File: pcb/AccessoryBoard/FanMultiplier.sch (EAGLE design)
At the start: 22 parts

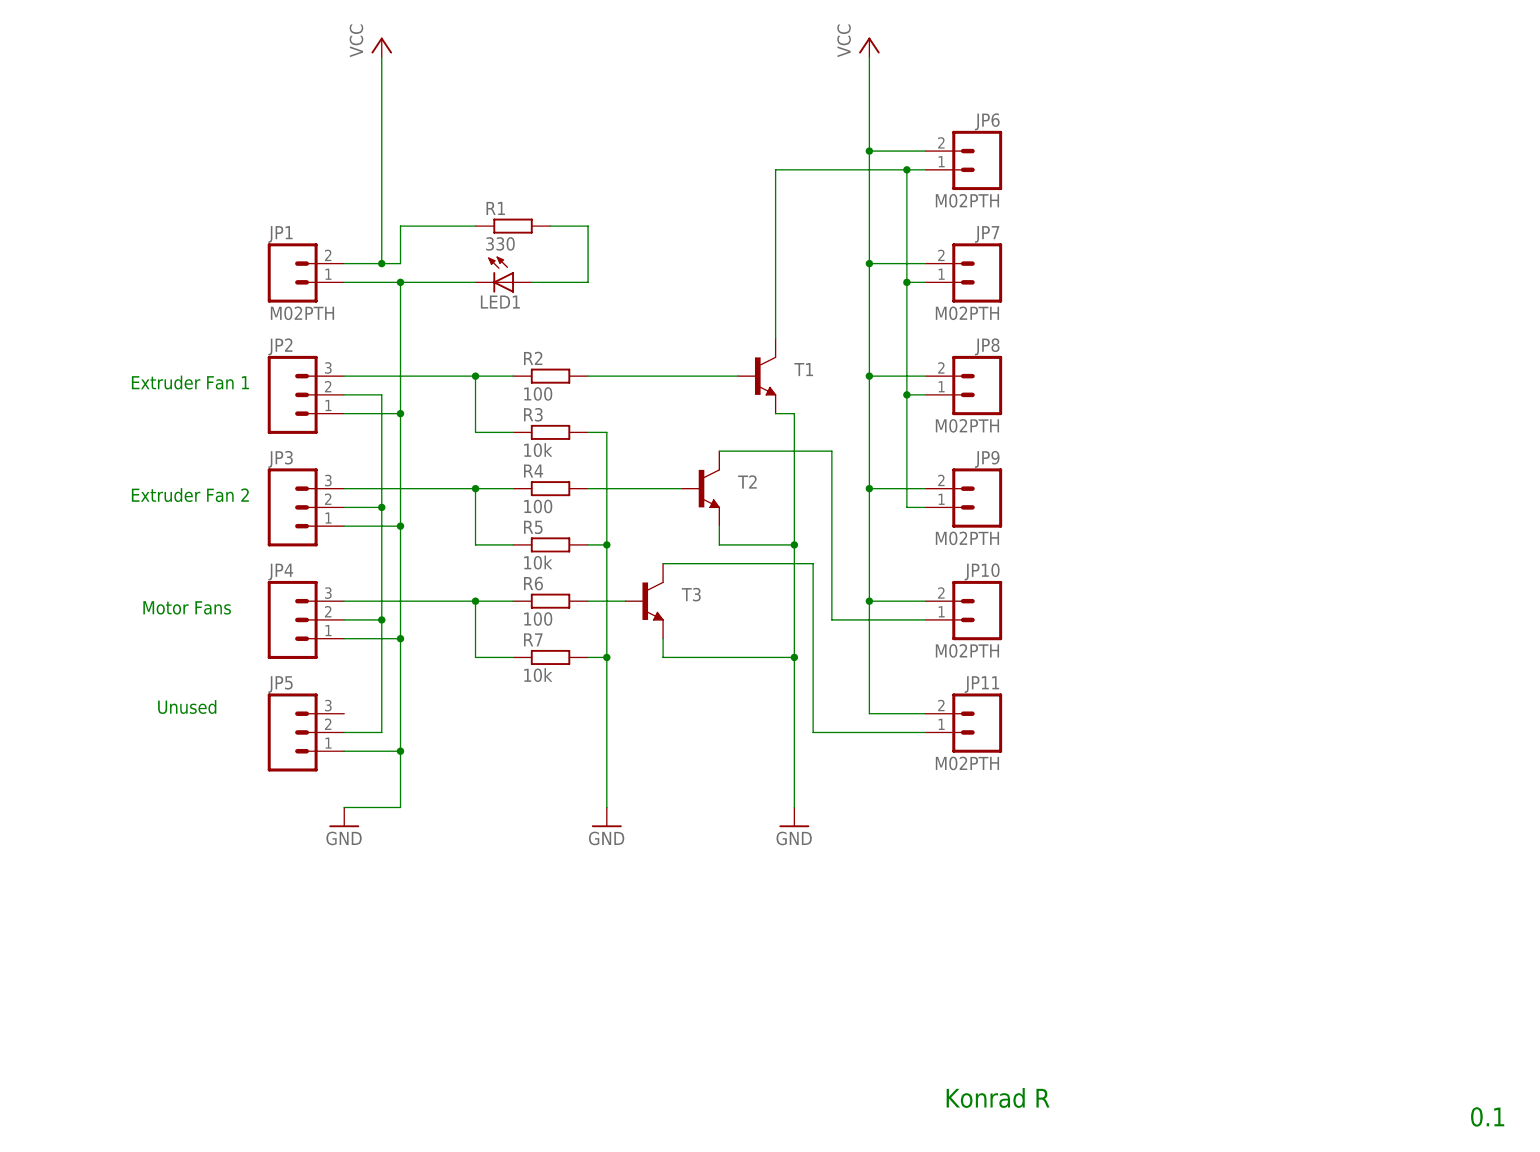
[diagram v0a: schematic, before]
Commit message: added vcc outputs added 4th pwm output
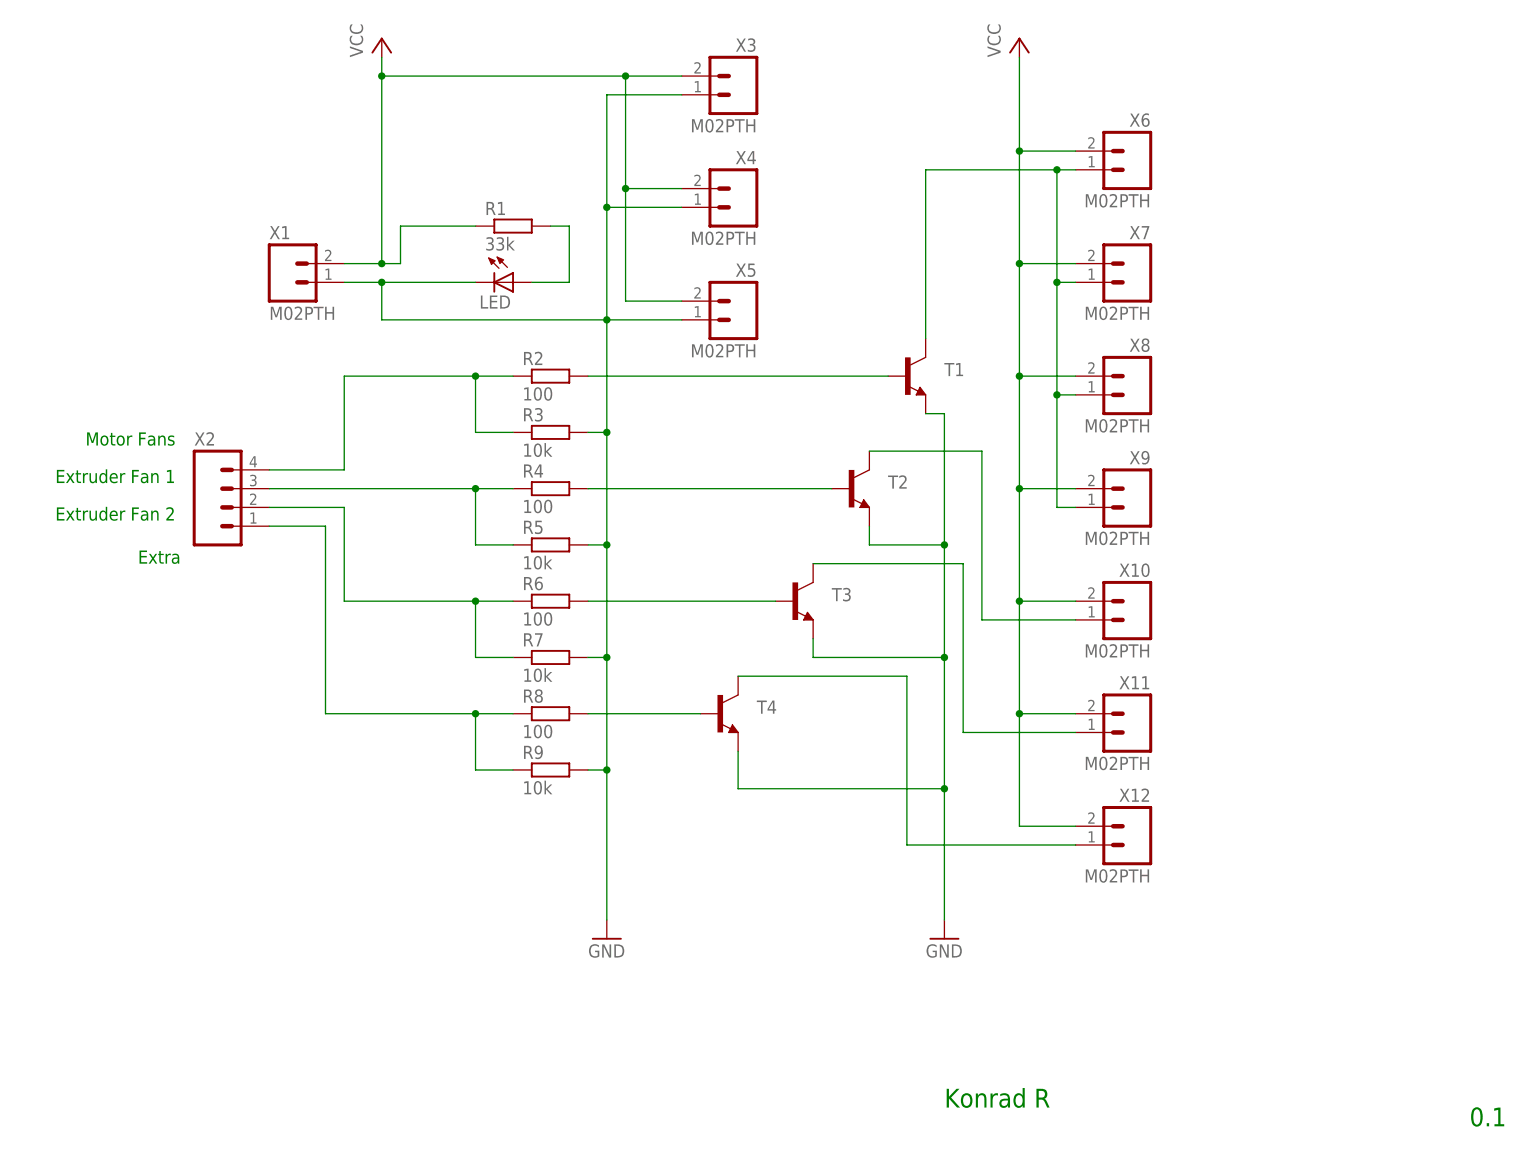
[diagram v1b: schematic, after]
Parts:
- removed JP10, JP11, JP6, JP7, JP8, JP9: M02PTH, SparkFun-Connectors:M02PTH
- removed JP2, JP3, JP4, JP5: (no value), SparkFun-Connectors:M03PTH
- added R8: 100, rcl:R-EU_0207/7
- added R9: 10k, rcl:R-EU_0207/7
- added T4: (no value), SparkFun-DiscreteSemi:TRANSISTOR_NPNTO92
- added X10, X11, X12, X3, X4, X5, X6, X7, X8, X9: M02PTH, SparkFun-Connectors:M02PTH
- added X2: (no value), SparkFun-Connectors:M04PTH
- R1: value 330 -> 33k
- renumbered JP1 to X1, LED1 to LED
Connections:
- new net N$11: R8.2, T4.B
- new net N$12: T4.C, X12.1
- net GND: now also R9.2, T4.E, X3.1, X4.1, X5.1; no longer JP2.1, JP3.1, JP4.1, JP5.1
- net N$14: now also X6.1, X7.1, X8.1, X9.1; no longer JP6.1, JP7.1, JP8.1, JP9.1
- net N$16: now also X10.1; no longer JP10.1
- net N$17: now also X11.1; no longer JP11.1
- net N$5: now also X2.4; no longer JP2.3
- net N$6: now also X2.3; no longer JP3.3
- net N$7: now also X2.2; no longer JP4.3
- net N$8: now also R8.1, R9.1, X2.1; no longer JP2.2, JP3.2, JP4.2, JP5.2
- net VCC: now also X10.2, X11.2, X12.2, X3.2, X4.2, X5.2, X6.2, X7.2, X8.2, X9.2; no longer JP10.2, JP11.2, JP6.2, JP7.2, JP8.2, JP9.2
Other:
- note added: "Extra"
- note removed: "Unused"
- moved on the sheet: T1, T2, T3

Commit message: minor routing improvements
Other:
- note added: "Nova Labs Fan Board"
- note added: "Version 2013/11/27"
- note removed: "0.1"
- note removed: "Konrad R"
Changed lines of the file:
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@@
 <grid distance="0.1" unitdist="inch" unit="inch" style="lines" multiple="1" display="no" altdistance="0.01" altunitdist="inch" altunit="inch"/>
 <layers>
-<layer number="1" name="Top" color="4" fill="1" visible="yes" active="no"/>
-<layer number="16" name="Bottom" color="1" fill="1" visible="yes" active="no"/>
-<layer number="17" name="Pads" color="2" fill="1" visible="yes" active="no"/>
-<layer number="18" name="Vias" color="2" fill="1" visible="yes" active="no"/>
-<layer number="19" name="Unrouted" color="6" fill="1" visible="yes" active="no"/>
-<layer number="20" name="Dimension" color="15" fill="1" visible="yes" active="no"/>
-<layer number="21" name="tPlace" color="7" fill="1" visible="yes" active="no"/>
-<layer number="22" name="bPlace" color="7" fill="1" visible="yes" active="no"/>
-<layer number="23" name="tOrigins" color="15" fill="1" visible="yes" active="no"/>
-<layer number="24" name="bOrigins" color="15" fill="1" visible="yes" active="no"/>
-<layer number="25" name="tNames" color="7" fill="1" visible="yes" active="no"/>
-<layer number="26" name="bNames" color="7" fill="1" visible="yes" active="no"/>
-<layer number="27" name="tValues" color="7" fill="1" visible="yes" active="no"/>
-<layer number="28" name="bValues" color="7" fill="1" visible="yes" active="no"/>
+<layer number="1" name="Top" color="4" fill="1" visible="no" active="no"/>
+<layer number="16" name="Bottom" color="1" fill="1" visible="no" active="no"/>
+<layer number="17" name="Pads" color="2" fill="1" visible="no" active="no"/>
+<layer number="18" name="Vias" color="2" fill="1" visible="no" active="no"/>
+<layer number="19" name="Unrouted" color="6" fill="1" visible="no" active="no"/>
+<layer number="20" name="Dimension" color="15" fill="1" visible="no" active="no"/>
+<layer number="21" name="tPlace" color="7" fill="1" visible="no" active="no"/>
+<layer number="22" name="bPlace" color="7" fill="1" visible="no" active="no"/>
+<layer number="23" name="tOrigins" color="15" fill="1" visible="no" active="no"/>
+<layer number="24" name="bOrigins" color="15" fill="1" visible="no" active="no"/>
+<layer number="25" name="tNames" color="7" fill="1" visible="no" active="no"/>
+<layer number="26" name="bNames" color="7" fill="1" visible="no" active="no"/>
+<layer number="27" name="tValues" color="7" fill="1" visible="no" active="no"/>
+<layer number="28" name="bValues" color="7" fill="1" visible="no" active="no"/>
 <layer number="29" name="tStop" color="7" fill="3" visible="no" active="no"/>
 <layer number="30" name="bStop" color="7" fill="6" visible="no" active="no"/>
@@
 <layer number="35" name="tGlue" color="7" fill="4" visible="no" active="no"/>
 <layer number="36" name="bGlue" color="7" fill="5" visible="no" active="no"/>
-<layer number="37" name="tTest" color="7" fill="1" visible="yes" active="no"/>
-<layer number="38" name="bTest" color="7" fill="1" visible="yes" active="no"/>
+<layer number="37" name="tTest" color="7" fill="1" visible="no" active="no"/>
+<layer number="38" name="bTest" color="7" fill="1" visible="no" active="no"/>
 <layer number="39" name="tKeepout" color="4" fill="11" visible="no" active="no"/>
 <layer number="40" name="bKeepout" color="1" fill="11" visible="no" active="no"/>
@@
 <layer number="44" name="Drills" color="7" fill="1" visible="no" active="no"/>
 <layer number="45" name="Holes" color="7" fill="1" visible="no" active="no"/>
-<layer number="46" name="Milling" color="3" fill="1" visible="yes" active="no"/>
-<layer number="47" name="Measures" color="7" fill="1" visible="yes" active="no"/>
-<layer number="48" name="Document" color="7" fill="1" visible="yes" active="no"/>
-<layer number="49" name="Reference" color="7" fill="1" visible="yes" active="no"/>
-<layer number="50" name="dxf" color="7" fill="1" visible="yes" active="no"/>
-<layer number="51" name="tDocu" color="7" fill="1" visible="yes" active="no"/>
-<layer number="52" name="bDocu" color="7" fill="1" visible="yes" active="no"/>
-<layer number="53" name="tGND_GNDA" color="7" fill="9" visible="yes" active="no"/>
-<layer number="54" name="bGND_GNDA" color="1" fill="9" visible="yes" active="no"/>
-<layer number="56" name="wert" color="7" fill="1" visible="yes" active="no"/>
+<layer number="46" name="Milling" color="3" fill="1" visible="no" active="no"/>
+<layer number="47" name="Measures" color="7" fill="1" visible="no" active="no"/>
+<layer number="48" name="Document" color="7" fill="1" visible="no" active="no"/>
+<layer number="49" name="Reference" color="7" fill="1" visible="no" active="no"/>
+<layer number="50" name="dxf" color="7" fill="1" visible="no" active="no"/>
+<layer number="51" name="tDocu" color="7" fill="1" visible="no" active="no"/>
+<layer number="52" name="bDocu" color="7" fill="1" visible="no" active="no"/>
+<layer number="53" name="tGND_GNDA" color="7" fill="9" visible="no" active="no"/>
+<layer number="54" name="bGND_GNDA" color="1" fill="9" visible="no" active="no"/>
+<layer number="56" name="wert" color="7" fill="1" visible="no" active="no"/>
 <layer number="91" name="Nets" color="2" fill="1" visible="yes" active="yes"/>
 <layer number="92" name="Busses" color="1" fill="1" visible="yes" active="yes"/>
@@
 <text x="63.5" y="101.6" size="1.778" layer="91" rot="R180">Motor Fans</text>
 <text x="58.42" y="83.82" size="1.778" layer="91">Extra</text>
-<text x="167.64" y="10.16" size="2.54" layer="91">Konrad R</text>
-<text x="238.76" y="7.62" size="2.54" layer="91">0.1</text>
+<text x="48.26" y="48.26" size="2.54" layer="91">Nova Labs Fan Board</text>
+<text x="48.26" y="43.18" size="1.778" layer="91">Version 2013/11/27</text>
 </plain>
 <instances>
@@
 <instance part="P+1" gate="VCC" x="91.44" y="154.94"/>
 <instance part="P+2" gate="VCC" x="177.8" y="154.94"/>
-<instance part="GND1" gate="1" x="167.64" y="33.02"/>
+<instance part="GND1" gate="1" x="167.64" y="40.64"/>
 <instance part="X1" gate="G$1" x="78.74" y="121.92"/>
 <instance part="T3" gate="G$1" x="147.32" y="78.74"/>
@@
 <instance part="X10" gate="G$1" x="193.04" y="76.2" rot="MR0"/>
 <instance part="X11" gate="G$1" x="193.04" y="60.96" rot="MR0"/>
-<instance part="GND3" gate="1" x="121.92" y="33.02"/>
+<instance part="GND3" gate="1" x="121.92" y="40.64"/>
 <instance part="LED" gate="G$1" x="109.22" y="121.92" rot="R270"/>
 <instance part="R1" gate="G$1" x="109.22" y="129.54"/>
@@
 <wire x1="121.92" y1="71.12" x2="121.92" y2="55.88" width="0.1524" layer="91"/>
 <pinref part="R5" gate="G$1" pin="2"/>
-<wire x1="121.92" y1="55.88" x2="121.92" y2="35.56" width="0.1524" layer="91"/>
+<wire x1="121.92" y1="55.88" x2="121.92" y2="43.18" width="0.1524" layer="91"/>
 <wire x1="119.38" y1="86.36" x2="121.92" y2="86.36" width="0.1524" layer="91"/>
 <wire x1="121.92" y1="86.36" x2="121.92" y2="71.12" width="0.1524" layer="91"/>
@@
 <pinref part="GND1" gate="1" pin="GND"/>
 <pinref part="T3" gate="G$1" pin="E"/>
-<wire x1="167.64" y1="35.56" x2="167.64" y2="53.34" width="0.1524" layer="91"/>
+<wire x1="167.64" y1="43.18" x2="167.64" y2="53.34" width="0.1524" layer="91"/>
 <wire x1="167.64" y1="53.34" x2="167.64" y2="71.12" width="0.1524" layer="91"/>
 <wire x1="167.64" y1="71.12" x2="149.86" y2="71.12" width="0.1524" layer="91"/>
